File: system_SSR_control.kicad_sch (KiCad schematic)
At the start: 13 parts, among them Q1 2.1V, Q2 2N7000, Q3 2N7000, SW1 FSM2JSMA, SW2 FSM2JSMA

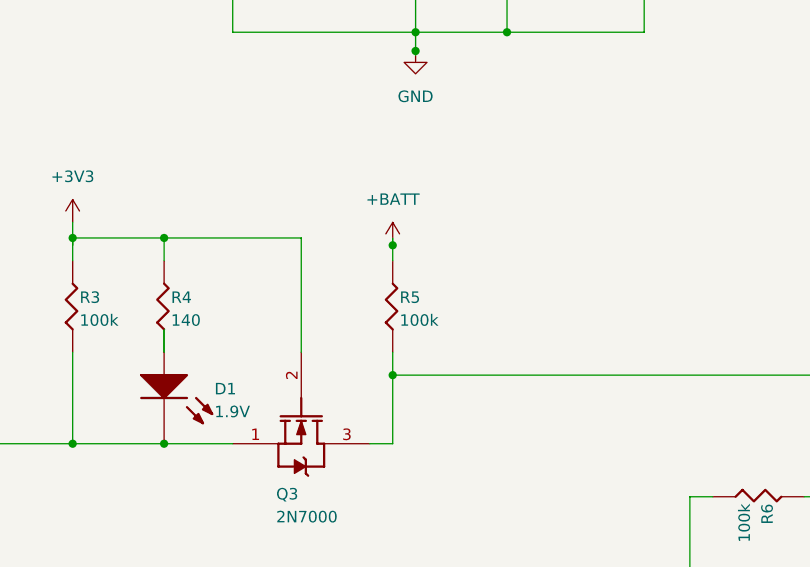
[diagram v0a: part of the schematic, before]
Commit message: Removed battery power and input header
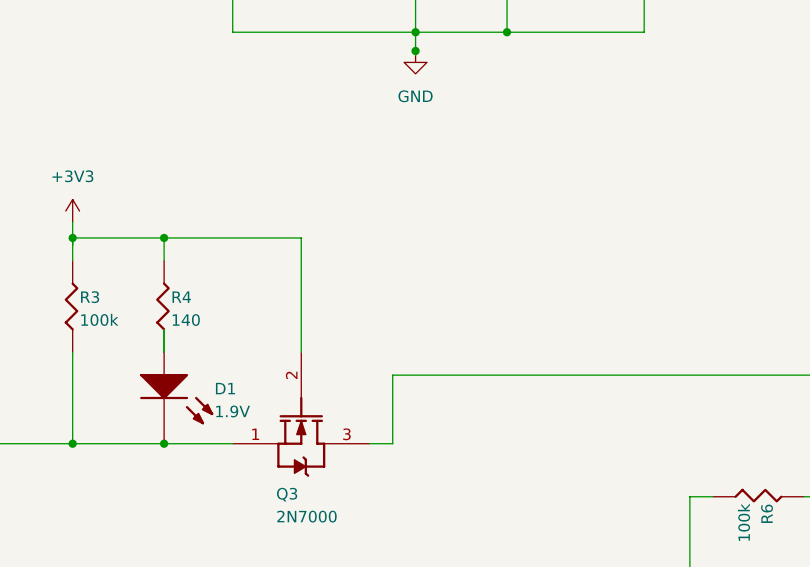
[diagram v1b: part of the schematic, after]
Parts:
- removed R5: 100k, Resistor_SMD:R_0805_2012Metric_Pad1.20x1.40mm_HandSolder, symbol MEB-altium-import:system_SSR_control_1_ERJ-6ENF1003V
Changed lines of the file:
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@@
   (junction (at 101.6 138.8872) (diameter 0) (color 0 0 0 0)
   )
-  (junction (at 137.16 139.7) (diameter 0) (color 0 0 0 0)
-  )
   (junction (at 165.1 83.82) (diameter 0) (color 0 0 0 0)
   )
@@
   )
   (junction (at 139.7 83.0072) (diameter 0) (color 0 0 0 0)
-  )
-  (junction (at 137.16 154.1272) (diameter 0) (color 0 0 0 0)
   )
   (junction (at 119.38 110.9472) (diameter 0) (color 0 0 0 0)
@@
     (stroke (width 0.254) (type default))
   )
-  (wire (pts (xy 137.16 151.5872) (xy 137.16 154.1272))
-    (stroke (width 0.254) (type default))
-  )
   (wire (pts (xy 129.54 83.0072) (xy 119.38 83.0072))
     (stroke (width 0.254) (type default))
@@
     (stroke (width 0.254) (type default))
   )
-  (wire (pts (xy 137.16 138.8872) (xy 137.16 139.7))
-    (stroke (width 0.254) (type default))
-  )
   (wire (pts (xy 165.1 110.9472) (xy 165.1 116.0272))
     (stroke (width 0.254) (type default))
@@
   )
   (wire (pts (xy 116.84 110.9472) (xy 119.38 110.9472))
-    (stroke (width 0.254) (type default))
-  )
-  (wire (pts (xy 137.16 139.7) (xy 137.16 141.4272))
     (stroke (width 0.254) (type default))
   )
@@
     )
   )
-  (symbol (lib_id "power:+BATT") (at 137.16 139.7 0) (unit 1)
-    (in_bom yes) (on_board yes) (dnp no) (fields_autoplaced)
-    (property "Reference" "#PWR041" (at 137.16 143.51 0)
-      (effects (font (size 1.27 1.27)) hide)
-    )
-    (property "Value" "+BATT" (at 137.16 134.62 0)
-      (effects (font (size 1.27 1.27)))
-    )
-    (property "Footprint" "" (at 137.16 139.7 0)
-      (effects (font (size 1.27 1.27)) hide)
-    )
-    (property "Datasheet" "" (at 137.16 139.7 0)
-      (effects (font (size 1.27 1.27)) hide)
-    )
-    (pin "1")
-    (instances
-      (project "MEB"
-        (path "/228e4997-23c1-4c21-939b-583cad26a5e3"
-          (reference "#PWR041") (unit 1)
-        )
-        (path "/228e4997-23c1-4c21-939b-583cad26a5e3/d2748488-1aa2-4890-bfa9-60c09f864312"
-          (reference "#PWR042") (unit 1)
-        )
-      )
-    )
-  )
   (symbol (lib_id "MEB-altium-import:system_SSR_control_1_ERJ-6ENF1003V") (at 186.69 161.29 0) (unit 1)
     (in_bom yes) (on_board yes) (dnp no)
@@
         )
       )
-    )
-  )
-  (symbol (lib_id "MEB-altium-import:system_SSR_control_1_ERJ-6ENF1003V") (at 137.16 146.5072 0) (unit 1)
-    (in_bom yes) (on_board yes) (dnp no)
-    (property "Reference" "R5" (at 137.922 146.2532 0)
-      (effects (font (size 1.27 1.27)) (justify left bottom))
-    )
-    (property "Value" "100k" (at 137.922 148.7932 0)
-      (effects (font (size 1.27 1.27)) (justify left bottom))
-    )
-    (property "Footprint" "Resistor_SMD:R_0805_2012Metric_Pad1.20x1.40mm_HandSolder" (at 137.16 146.5072 0)
-      (effects (font (size 1.27 1.27)) hide)
-    )
-    (property "Datasheet" "" (at 137.16 146.5072 0)
-      (effects (font (size 1.27 1.27)) hide)
-    )
-    (property "Part Number" "ERJ-6ENF1003V" (at 137.16 146.5072 0)
-      (effects (font (size 1.27 1.27)) hide)
-    )
-    (pin "1")
-    (pin "2")
-    (instances
-      (project "MEB"
-        (path "/228e4997-23c1-4c21-939b-583cad26a5e3/d2748488-1aa2-4890-bfa9-60c09f864312"
-          (reference "R5") (unit 1)
-        )
-      )

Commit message: Fix a variety of small issues
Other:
- moved on the sheet: D1, Q1, Q2, Q3, R1, R2, R25, R3, R4, R6, SW1, SW2
